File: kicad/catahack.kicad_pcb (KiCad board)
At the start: 4 copper layers, 100 x 100 mm, 109 parts, among them J1 XCVR power choice, J10 PC_AUDIO_EXTRA, J11 Jack header, J12 Jack header, J13 L/R channel choice, J14 Jack header, J15 CITA/OMTP choice, J16 TRRS/TRS+TS choice, J17 Audio header, J18 Xcvr grounding jumpers, J19 XCVR_Audio, J2 USB_B, J3 FTDI header, J4 PTT choice, J5 XCVR_CAT_TTL, J6 XCVR_PTT, J7 XCVR_CAT_RS232, J8 PC_AUDIO_IO, J9 PC_AUDIO_OUT, T1 T6003NL, T2 T6003NL, U1 PQS075-S5-S5-S, U2 L78M05CDT-TR, U3 SN65220, U4 Si8663AB-B-IS1, U5 FT232RL, U6 SN74HCT32D, U7 VOR1121B6T, U8 MAX3387ECUG+

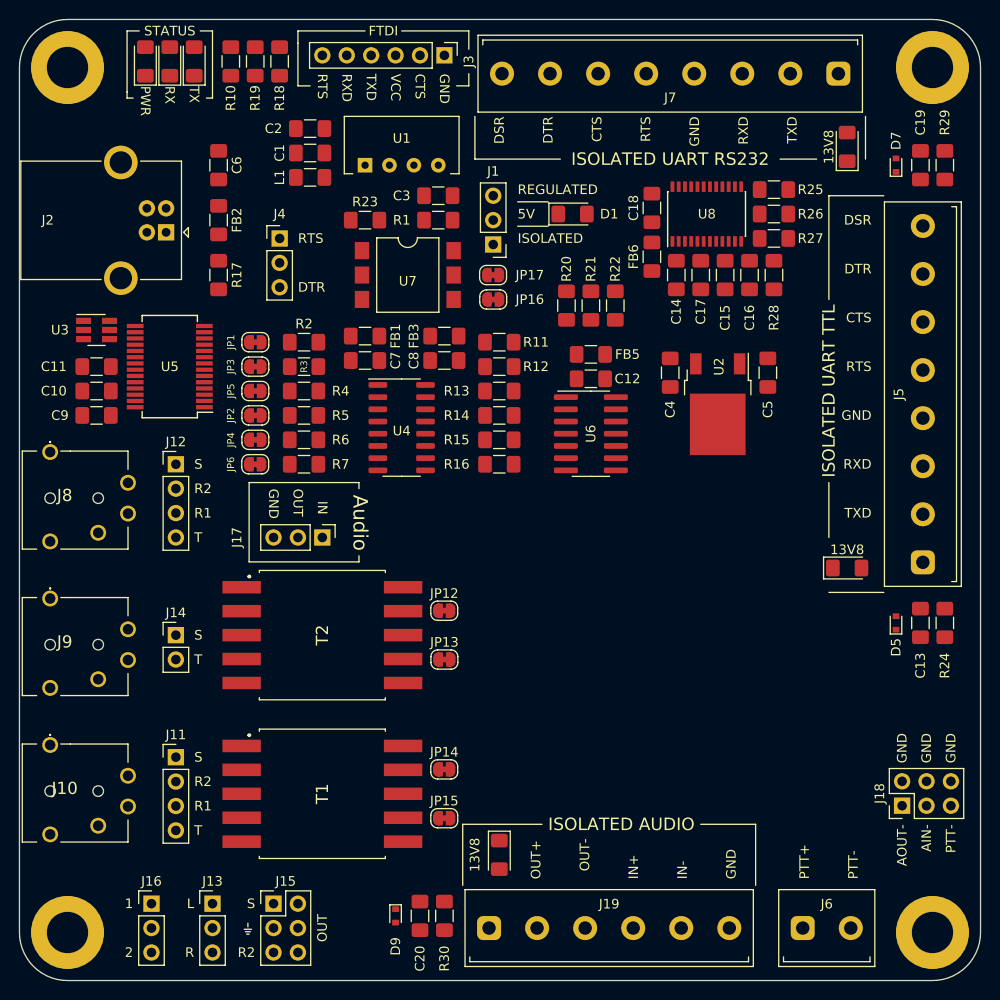
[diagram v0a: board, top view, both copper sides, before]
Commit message: New layout, routing, misc...
* Redo layout
* Fixed MAX pulldown resistors on data lines.
* Added jumpers in case MAX not installed.
* Remove audio header
* Remove some redundant solder jumpers
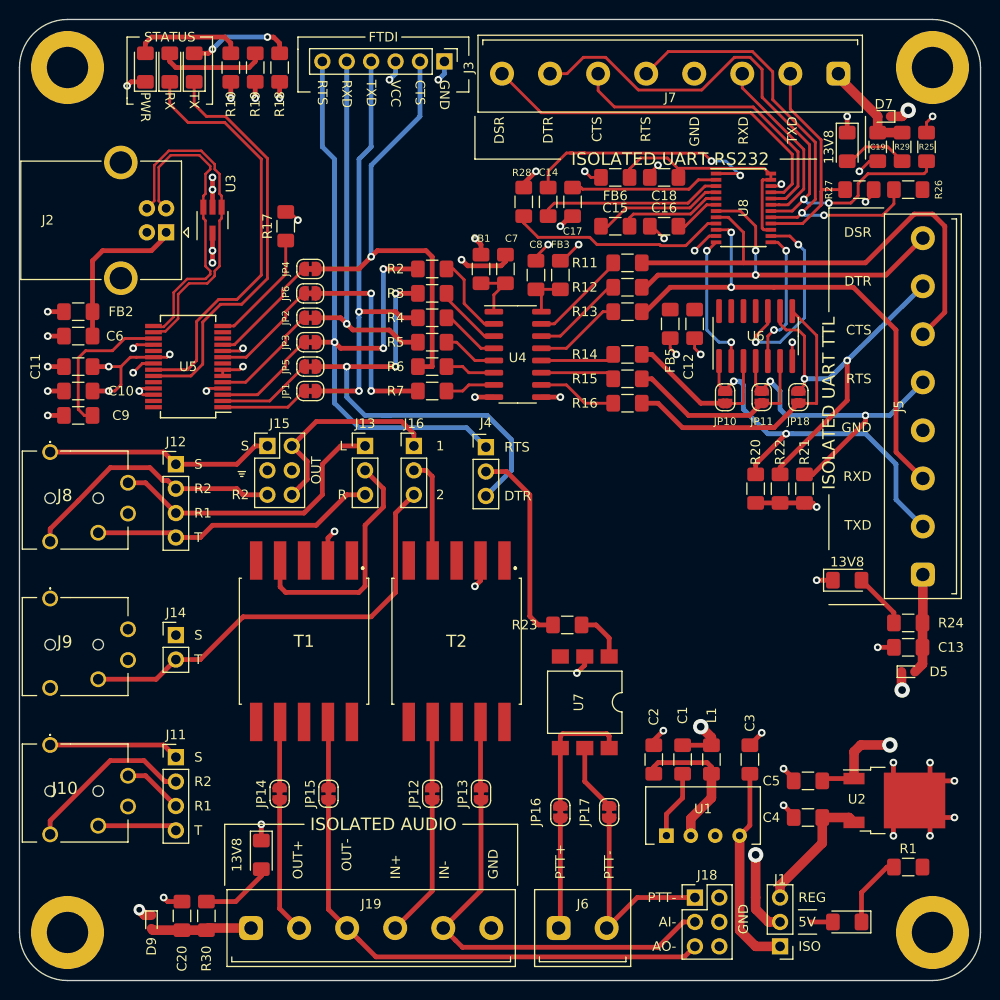
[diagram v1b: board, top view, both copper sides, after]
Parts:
- removed J17: Audio header, Connector_PinHeader_2.54mm:PinHeader_1x03_P2.54mm_Vertical
- added JP10: SolderJumper_2_Open, Jumper:SolderJumper-2_P1.3mm_Open_RoundedPad1.0x1.5mm, F.Cu at (98.4, 74.3)
- added JP11: SolderJumper_2_Open, Jumper:SolderJumper-2_P1.3mm_Open_RoundedPad1.0x1.5mm, F.Cu at (102.2, 74.3)
- added JP18: SolderJumper_2_Open, Jumper:SolderJumper-2_P1.3mm_Open_RoundedPad1.0x1.5mm, F.Cu at (106.0, 74.3)
- moved R1 83.2 mm to (117.5, 123.2), turned to 0 degrees
- moved D1 79.0 mm to (111.1, 128.9), turned to 180 degrees
- moved J1 78.9 mm to (104.1, 131.4)
- moved U1 76.5 mm to (96.1, 119.9)
- moved C2 74.8 mm to (91.0, 112.0), turned to 270 degrees
- moved C1 74.1 mm to (94.0, 112.0), turned to 90 degrees
- moved L1 73.6 mm to (97.0, 112.0), turned to 90 degrees
- moved C3 67.0 mm to (101.0, 112.0), turned to 270 degrees
- moved JP17 57.2 mm to (86.4, 117.5), turned to 270 degrees
- moved J16 54.9 mm to (66.0, 79.4)
- moved JP16 53.8 mm to (81.3, 117.5), turned to 270 degrees
- moved J13 50.2 mm to (61.0, 79.4)
- moved C4 48.4 mm to (107.0, 118.0), turned to 180 degrees
- moved U7 48.1 mm to (83.8, 106.0), turned to 270 degrees
- moved J15 47.6 mm to (50.8, 79.4)
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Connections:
- J18 pad 1: Net-(J18-Pad1) -> XCVR_PTT-
- J18 pad 5: XCVR_PTT- -> Net-(J18-Pad5)
- J19 pad 3: Net-(J18-Pad1) -> Net-(J18-Pad5)
- J5 pad 3: /data/XCVR_RXD -> XCVR_RXD
- J5 pad 6: /data/XCVR_CTS -> XCVR_CTS
- J5 pad 8: /data/XCVR_DSR -> XCVR_DSR
- JP1 pad 1: /data/TXD -> Net-(JP1-Pad1)
- JP1 pad 2: Net-(JP1-Pad2) -> /data/TXD
- JP15 pad 2: Net-(J18-Pad1) -> Net-(J18-Pad5)
- JP2 pad 1: /data/RXD -> Net-(JP2-Pad1)
- JP2 pad 2: Net-(JP2-Pad2) -> /data/RXD
- JP3 pad 1: /data/RTS -> Net-(JP3-Pad1)
- JP3 pad 2: Net-(JP3-Pad2) -> /data/RTS
- JP4 pad 1: /data/CTS -> Net-(JP4-Pad1)
- JP4 pad 2: Net-(JP4-Pad2) -> /data/CTS
- JP5 pad 1: /data/DTR -> Net-(JP5-Pad1)
- JP5 pad 2: Net-(JP5-Pad2) -> /data/DTR
- JP6 pad 1: /data/DSR -> Net-(JP6-Pad1)
- JP6 pad 2: Net-(JP6-Pad2) -> /data/DSR
- R11 pad 1: /data/XCVR_RXD -> XCVR_CTS
- R12 pad 1: /data/XCVR_CTS -> XCVR_DSR
- R13 pad 1: /data/XCVR_DSR -> XCVR_RXD
- R2 pad 2: /data/TXD -> /data/RTS
- R25 pad 1: XCVR_TXD_DRV -> /data/rs232/RS232_DTR
- R26 pad 1: XCVR_RTS_DRV -> /data/rs232/RS232_RTS
- R27 pad 1: XCVR_DTR_DRV -> /data/rs232/RS232_TXD
- R3 pad 2: /data/RTS -> /data/DTR
- R4 pad 2: /data/DTR -> /data/TXD
- T1 pad 2: /audio/AUDIO_IN -> PC_AUDIO_GND
- T1 pad 4: PC_AUDIO_GND -> /audio/AUDIO_IN
- T1 pad 7: /audio/XCVR_AUDIO_OUT- -> /audio/XCVR_AUDIO_OUT+
- T1 pad 9: /audio/XCVR_AUDIO_OUT+ -> /audio/XCVR_AUDIO_OUT-
- T2 pad 2: /audio/AUDIO_OUT -> PC_AUDIO_GND
- T2 pad 4: PC_AUDIO_GND -> /audio/AUDIO_OUT
- T2 pad 7: /audio/XCVR_AUDIO_IN- -> /audio/XCVR_AUDIO_IN+
- T2 pad 9: /audio/XCVR_AUDIO_IN+ -> /audio/XCVR_AUDIO_IN-
- U5 pad 1: /data/TXD -> Net-(JP1-Pad1)
- U5 pad 11: /data/CTS -> Net-(JP4-Pad1)
- U5 pad 2: /data/DTR -> Net-(JP5-Pad1)
- U5 pad 3: /data/RTS -> Net-(JP3-Pad1)
- U5 pad 5: /data/RXD -> Net-(JP2-Pad1)
- U5 pad 9: /data/DSR -> Net-(JP6-Pad1)
- U8 pad 10: /data/rs232/XCVR_DSR -> XCVR_RXD
- U8 pad 12: XCVR_DTR_DRV -> XCVR_TXD_DRV
- U8 pad 14: XCVR_TXD_DRV -> XCVR_DTR_DRV
- U8 pad 16: /data/rs232/RS232_DTR -> /data/rs232/RS232_TXD
- U8 pad 18: /data/rs232/RS232_TXD -> /data/rs232/RS232_DTR
- U8 pad 19: /data/rs232/RS232_DSR -> /data/rs232/RS232_RXD
- U8 pad 21: /data/rs232/RS232_RXD -> /data/rs232/RS232_DSR
- U8 pad 7: /data/rs232/XCVR_RXD -> XCVR_DSR
- U8 pad 8: /data/rs232/XCVR_CTS -> XCVR_CTS
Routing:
- net XCVR_GND: track 0.00 -> 75.1 mm, vias 0 -> 28
- net /data/RTS: track 0.00 -> 72.8 mm, vias 0 -> 3
- net /data/rs232/RS232_DTR: track 0.00 -> 62.0 mm, vias 0 -> 2
- net XCVR_RXD: track 0.00 -> 53.4 mm, vias 0 -> 2
- net XCVR_CTS: track 0.00 -> 53.0 mm
- net Net-(J18-Pad5): track 0.00 -> 52.0 mm
- net GND: track 0.00 -> 49.2 mm, vias 0 -> 19
- net /data/CTS: track 0.00 -> 48.4 mm, vias 0 -> 1
- net /data/DTR: track 0.00 -> 47.9 mm, vias 0 -> 3
- net /data/rs232/RS232_RTS: track 0.00 -> 47.2 mm, vias 0 -> 2
- net Net-(J14-Pad2): track 0.00 -> 45.6 mm
- net /data/TXD: track 0.00 -> 45.6 mm, vias 0 -> 2
- net RXLED: track 0.00 -> 44.0 mm
- net TXLED: track 0.00 -> 43.4 mm
- net Net-(J18-Pad3): track 0.00 -> 43.1 mm
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- added copper zone on In1.Cu, net GND
- added copper zone on In1.Cu, net PC_AUDIO_GND
- added copper zone on In2.Cu, net VCC
- added copper zone on In2.Cu, net XCVR_13V8
- added copper zone on In2.Cu, net XCVR_5V
- added copper zone on In1.Cu, net XCVR_GND
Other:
- board text added: "AI-"
- board text added: "AO-"
- board text added: "ISO"
- board text added: "REG"
- board text removed: "AIN-"
- board text removed: "AOUT-"
- board text removed: "Audio"
- board text removed: "IN"
- board text removed: "ISOLATED"
- board text removed: "REGULATED"

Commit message: Logo and small corrections
* Added logo
* Connected a few unconnected pads
* Fixed GND pour intersection
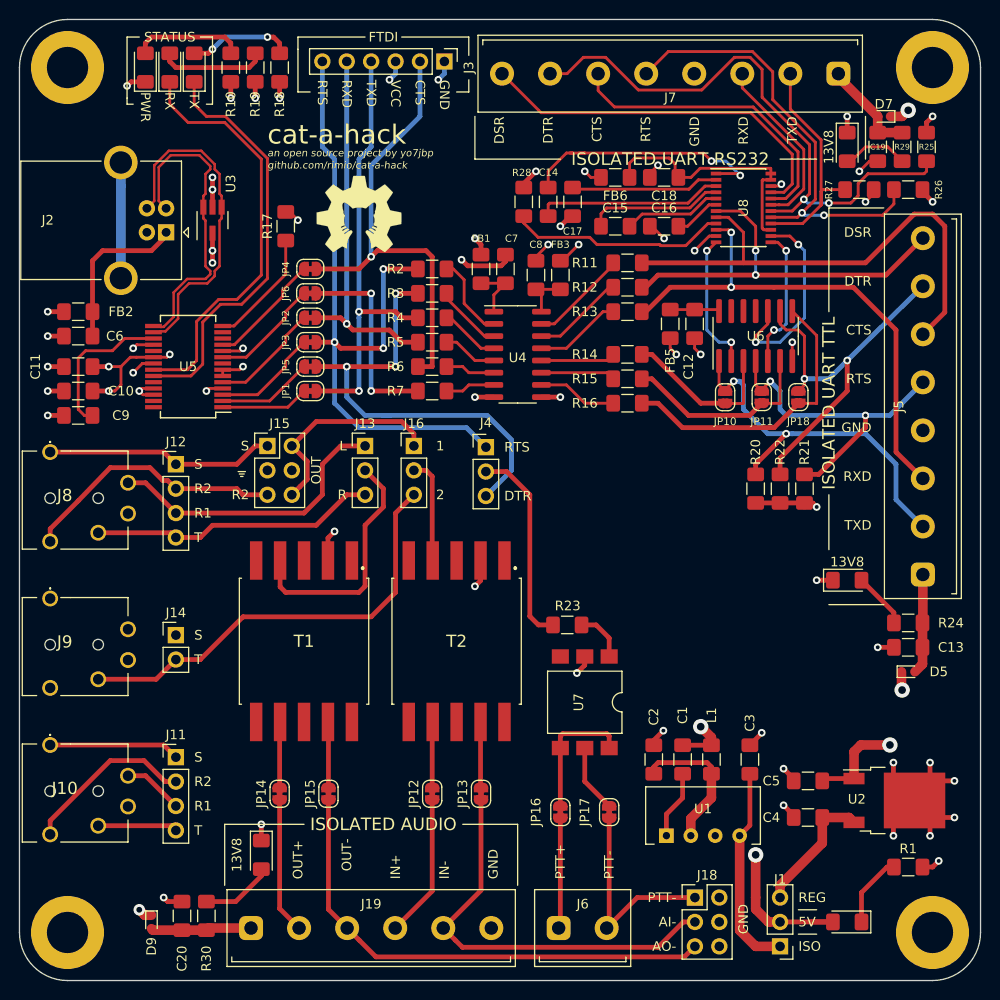
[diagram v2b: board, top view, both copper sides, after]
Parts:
- added G***: LOGO, logo:logo, F.Cu at (60.3, 55.2)
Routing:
- net Net-(J2-Pad5): track 0.00 -> 12.0 mm
- net XCVR_5V: track 17.6 -> 23.1 mm
- net Net-(C12-Pad2): track 0.00 -> 5.15 mm
- net XCVR_GND: track 75.1 -> 78.8 mm, vias 28 -> 30
- net Net-(C18-Pad2): track 25.0 -> 26.3 mm
- net Net-(C15-Pad1): track 13.4 -> 14.2 mm
- net Net-(C15-Pad2): track 10.7 -> 10.2 mm
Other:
- board text added: "an open source project by yo7jbp"
- board text added: "cat-a-hack"
- board text added: "github.com/rimio/cat-a-hack"

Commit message: Audio filtering, hackable area, misc
* Added bypass caps and ferrites to audio lines
* Small rerouting
* Hackable area
* Added rev no
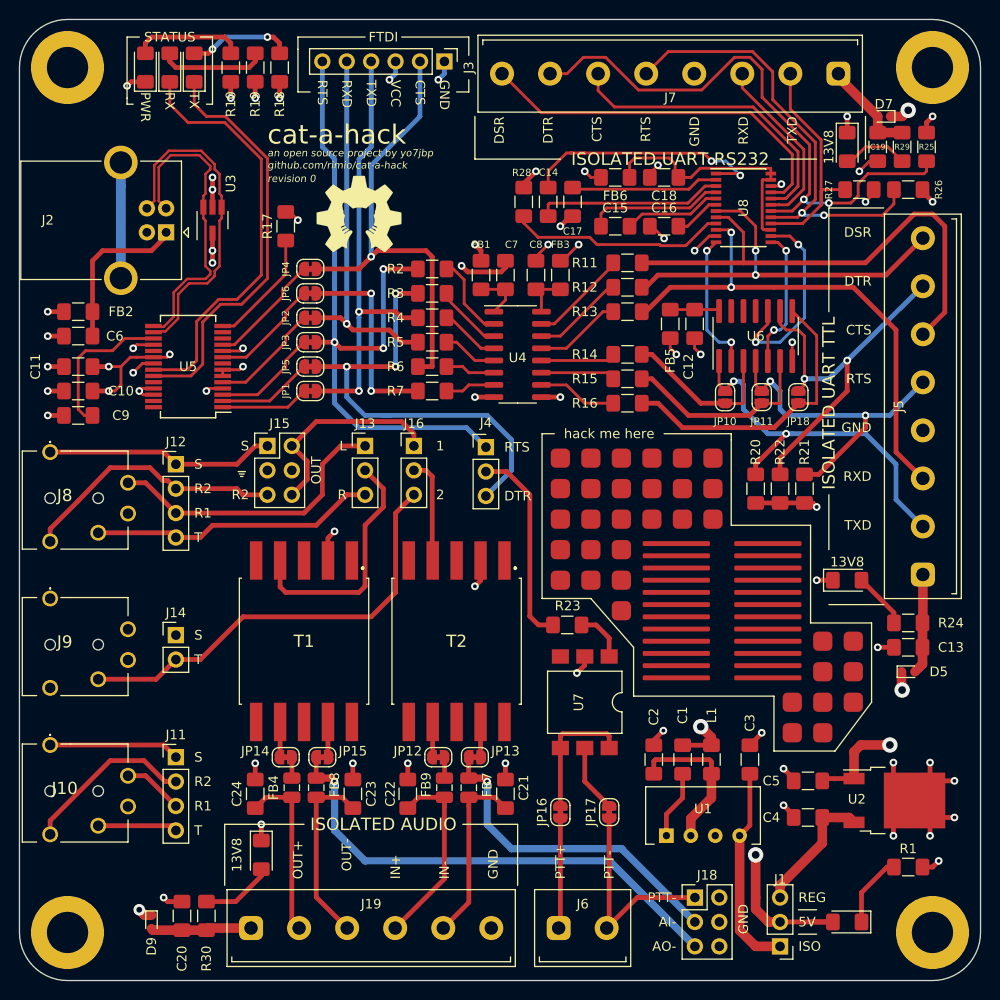
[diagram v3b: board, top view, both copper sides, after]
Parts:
- added C21: 27n, Capacitor_SMD:C_1206_3216Metric_Pad1.42x1.75mm_HandSolder, F.Cu at (75.6, 115.6)
- added C22: 27n, Capacitor_SMD:C_1206_3216Metric_Pad1.42x1.75mm_HandSolder, F.Cu at (65.4, 115.6)
- added C23: 27n, Capacitor_SMD:C_1206_3216Metric_Pad1.42x1.75mm_HandSolder, F.Cu at (59.7, 115.6)
- added C24: 27n, Capacitor_SMD:C_1206_3216Metric_Pad1.42x1.75mm_HandSolder, F.Cu at (49.5, 115.6)
- added FB4: NFZ2MSD101SZ10L, custom:NFZ2MSD101SZ10L_0806_Handsolder, F.Cu at (53.3, 114.9)
- added FB7: NFZ2MSD101SZ10L, custom:NFZ2MSD101SZ10L_0806_Handsolder, F.Cu at (71.8, 114.9)
- added FB8: NFZ2MSD101SZ10L, custom:NFZ2MSD101SZ10L_0806_Handsolder, F.Cu at (55.9, 114.9)
- added FB9: NFZ2MSD101SZ10L, custom:NFZ2MSD101SZ10L_0806_Handsolder, F.Cu at (69.2, 114.9)
- added REF**: Generic_Pad_SOP_7x0.51mm, custom:Generic_Pad_SOP_7x0.51mm, F.Cu at (102.9, 103.5)
- added REF**: Generic_Pad_SOP_7x0.51mm, custom:Generic_Pad_SOP_7x0.51mm, F.Cu at (93.3, 97.2)
- added REF**: Generic_Pad_SOP_7x0.51mm, custom:Generic_Pad_SOP_7x0.51mm, F.Cu at (93.3, 95.9)
- added REF**: Generic_Pad_SOP_7x0.51mm, custom:Generic_Pad_SOP_7x0.51mm, F.Cu at (102.9, 97.2)
- added REF**: Generic_Pad_SOP_7x0.51mm, custom:Generic_Pad_SOP_7x0.51mm, F.Cu at (93.3, 98.4)
- added REF**: Generic_Pad_SOP_7x0.51mm, custom:Generic_Pad_SOP_7x0.51mm, F.Cu at (102.9, 94.6)
- added REF**: Generic_Pad_SOP_7x0.51mm, custom:Generic_Pad_SOP_7x0.51mm, F.Cu at (93.3, 94.6)
- added REF**: Generic_Pad_SOP_7x0.51mm, custom:Generic_Pad_SOP_7x0.51mm, F.Cu at (102.9, 95.9)
- added REF**: Generic_Pad_SOP_7x0.51mm, custom:Generic_Pad_SOP_7x0.51mm, F.Cu at (102.9, 93.3)
- added REF**: Generic_Pad_SOP_7x0.51mm, custom:Generic_Pad_SOP_7x0.51mm, F.Cu at (93.3, 93.3)
- added REF**: Generic_Pad_SOP_7x0.51mm, custom:Generic_Pad_SOP_7x0.51mm, F.Cu at (102.9, 92.1)
- added REF**: Generic_Pad_SOP_7x0.51mm, custom:Generic_Pad_SOP_7x0.51mm, F.Cu at (93.3, 102.2)
- added REF**: Generic_Pad_SOP_7x0.51mm, custom:Generic_Pad_SOP_7x0.51mm, F.Cu at (93.3, 92.1)
- added REF**: Generic_Pad_SOP_7x0.51mm, custom:Generic_Pad_SOP_7x0.51mm, F.Cu at (102.9, 90.8)
- added REF**: Generic_Pad_SOP_7x0.51mm, custom:Generic_Pad_SOP_7x0.51mm, F.Cu at (93.3, 90.8)
- added REF**: Generic_Pad_SOP_7x0.51mm, custom:Generic_Pad_SOP_7x0.51mm, F.Cu at (102.9, 89.5)
- added REF**: Generic_Pad_SOP_7x0.51mm, custom:Generic_Pad_SOP_7x0.51mm, F.Cu at (93.3, 89.5)
- added REF**: Generic_Pad_2mm, custom:Generic_Pad_2mm, F.Cu at (105.4, 106.0)
- added REF**: Generic_Pad_2mm, custom:Generic_Pad_2mm, F.Cu at (87.6, 96.5)
- added REF**: Generic_Pad_2mm, custom:Generic_Pad_2mm, F.Cu at (108.6, 102.9)
- added REF**: Generic_Pad_2mm, custom:Generic_Pad_2mm, F.Cu at (108.6, 106.0)
- added REF**: Generic_Pad_2mm, custom:Generic_Pad_2mm, F.Cu at (108.6, 99.7)
- added REF**: Generic_Pad_SOP_7x0.51mm, custom:Generic_Pad_SOP_7x0.51mm, F.Cu at (93.3, 101.0)
- added REF**: Generic_Pad_2mm, custom:Generic_Pad_2mm, F.Cu at (111.8, 99.7)
- added REF**: Generic_Pad_2mm, custom:Generic_Pad_2mm, F.Cu at (105.4, 109.2)
- added REF**: Generic_Pad_2mm, custom:Generic_Pad_2mm, F.Cu at (111.8, 106.0)
- added REF**: Generic_Pad_2mm, custom:Generic_Pad_2mm, F.Cu at (111.8, 102.9)
- added REF**: Generic_Pad_2mm, custom:Generic_Pad_2mm, F.Cu at (108.6, 109.2)
- added REF**: Generic_Pad_2mm, custom:Generic_Pad_2mm, F.Cu at (81.3, 90.2)
- added REF**: Generic_Pad_2mm, custom:Generic_Pad_2mm, F.Cu at (87.6, 93.3)
- added REF**: Generic_Pad_2mm, custom:Generic_Pad_2mm, F.Cu at (87.6, 90.2)
- added REF**: Generic_Pad_2mm, custom:Generic_Pad_2mm, F.Cu at (84.5, 90.2)
- added REF**: Generic_Pad_2mm, custom:Generic_Pad_2mm, F.Cu at (84.5, 93.3)
- added REF**: Generic_Pad_SOP_7x0.51mm, custom:Generic_Pad_SOP_7x0.51mm, F.Cu at (102.9, 102.2)
- added REF**: Generic_Pad_2mm, custom:Generic_Pad_2mm, F.Cu at (81.3, 93.3)
- added REF**: Generic_Pad_2mm, custom:Generic_Pad_2mm, F.Cu at (81.3, 87.0)
- added REF**: Generic_Pad_2mm, custom:Generic_Pad_2mm, F.Cu at (97.2, 87.0)
- added REF**: Generic_Pad_2mm, custom:Generic_Pad_2mm, F.Cu at (87.6, 87.0)
- added REF**: Generic_Pad_2mm, custom:Generic_Pad_2mm, F.Cu at (84.5, 87.0)
- added REF**: Generic_Pad_2mm, custom:Generic_Pad_2mm, F.Cu at (94.0, 87.0)
- added REF**: Generic_Pad_2mm, custom:Generic_Pad_2mm, F.Cu at (90.8, 87.0)
- added REF**: Generic_Pad_2mm, custom:Generic_Pad_2mm, F.Cu at (81.3, 83.8)
- added REF**: Generic_Pad_2mm, custom:Generic_Pad_2mm, F.Cu at (97.2, 83.8)
- added REF**: Generic_Pad_2mm, custom:Generic_Pad_2mm, F.Cu at (87.6, 83.8)
- added REF**: Generic_Pad_SOP_7x0.51mm, custom:Generic_Pad_SOP_7x0.51mm, F.Cu at (93.3, 103.5)
- added REF**: Generic_Pad_2mm, custom:Generic_Pad_2mm, F.Cu at (84.5, 83.8)
- added REF**: Generic_Pad_2mm, custom:Generic_Pad_2mm, F.Cu at (94.0, 83.8)
- added REF**: Generic_Pad_2mm, custom:Generic_Pad_2mm, F.Cu at (90.8, 83.8)
- added REF**: Generic_Pad_2mm, custom:Generic_Pad_2mm, F.Cu at (97.2, 80.6)
- added REF**: Generic_Pad_2mm, custom:Generic_Pad_2mm, F.Cu at (94.0, 80.6)
- added REF**: Generic_Pad_2mm, custom:Generic_Pad_2mm, F.Cu at (90.8, 80.6)
- added REF**: Generic_Pad_2mm, custom:Generic_Pad_2mm, F.Cu at (87.6, 80.6)
- added REF**: Generic_Pad_2mm, custom:Generic_Pad_2mm, F.Cu at (84.5, 80.6)
- added REF**: Generic_Pad_2mm, custom:Generic_Pad_2mm, F.Cu at (81.3, 80.6)
- added REF**: Generic_Pad_SOP_7x0.51mm, custom:Generic_Pad_SOP_7x0.51mm, F.Cu at (102.9, 99.7)
- added REF**: Generic_Pad_SOP_7x0.51mm, custom:Generic_Pad_SOP_7x0.51mm, F.Cu at (93.3, 99.7)
- added REF**: Generic_Pad_SOP_7x0.51mm, custom:Generic_Pad_SOP_7x0.51mm, F.Cu at (102.9, 101.0)
- added REF**: Generic_Pad_SOP_7x0.51mm, custom:Generic_Pad_SOP_7x0.51mm, F.Cu at (102.9, 98.4)
- moved JP12 3.86 mm to (68.6, 111.8), turned to 0 degrees
- moved JP13 3.86 mm to (72.4, 111.8), turned to 180 degrees
- moved JP14 3.86 mm to (52.7, 111.8), turned to 0 degrees
- moved JP15 3.86 mm to (56.5, 111.8), turned to 180 degrees
- moved C7 0.63 mm to (75.6, 61.6)
- moved FB1 0.63 mm to (73.0, 61.6)
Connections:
- J18 pad 3: Net-(J18-Pad3) -> Net-(FB7-Pad2)
- J18 pad 5: Net-(J18-Pad5) -> Net-(FB8-Pad2)
- J19 pad 2: Net-(J19-Pad2) -> Net-(C24-Pad1)
- J19 pad 3: Net-(J18-Pad5) -> Net-(C23-Pad1)
- J19 pad 4: Net-(J19-Pad4) -> Net-(C22-Pad1)
- J19 pad 5: Net-(J18-Pad3) -> Net-(C21-Pad1)
- JP12 pad 2: Net-(J19-Pad4) -> Net-(FB9-Pad2)
- JP13 pad 2: Net-(J18-Pad3) -> Net-(FB7-Pad2)
- JP14 pad 2: Net-(J19-Pad2) -> Net-(FB4-Pad2)
- JP15 pad 2: Net-(J18-Pad5) -> Net-(FB8-Pad2)
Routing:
- net Net-(J18-Pad5): track 52.0 -> 0.00 mm
- net Net-(FB8-Pad2): track 0.00 -> 51.8 mm, vias 0 -> 1
- net Net-(J18-Pad3): track 43.1 -> 0.00 mm
- net Net-(FB7-Pad2): track 0.00 -> 34.5 mm, vias 0 -> 1
- net Net-(C22-Pad1): track 0.00 -> 20.0 mm
- net Net-(C23-Pad1): track 0.00 -> 19.2 mm
- net Net-(C21-Pad1): track 0.00 -> 19.0 mm
- net Net-(C24-Pad1): track 0.00 -> 18.2 mm
- net Net-(J19-Pad4): track 14.9 -> 0.00 mm
- net Net-(J19-Pad2): track 14.2 -> 0.00 mm
- net XCVR_GND: track 78.8 -> 85.5 mm, vias 30 -> 34
- net /audio/XCVR_AUDIO_IN+: track 6.85 -> 3.69 mm
- net /audio/XCVR_AUDIO_OUT-: track 6.85 -> 3.69 mm
- net /audio/XCVR_AUDIO_OUT+: track 6.85 -> 3.69 mm
- net /audio/XCVR_AUDIO_IN-: track 6.85 -> 3.69 mm
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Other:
- board text added: "hack me here"
- board text added: "revision 0"
